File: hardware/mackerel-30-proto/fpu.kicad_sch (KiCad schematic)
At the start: 10 parts, among them U11 MC68882

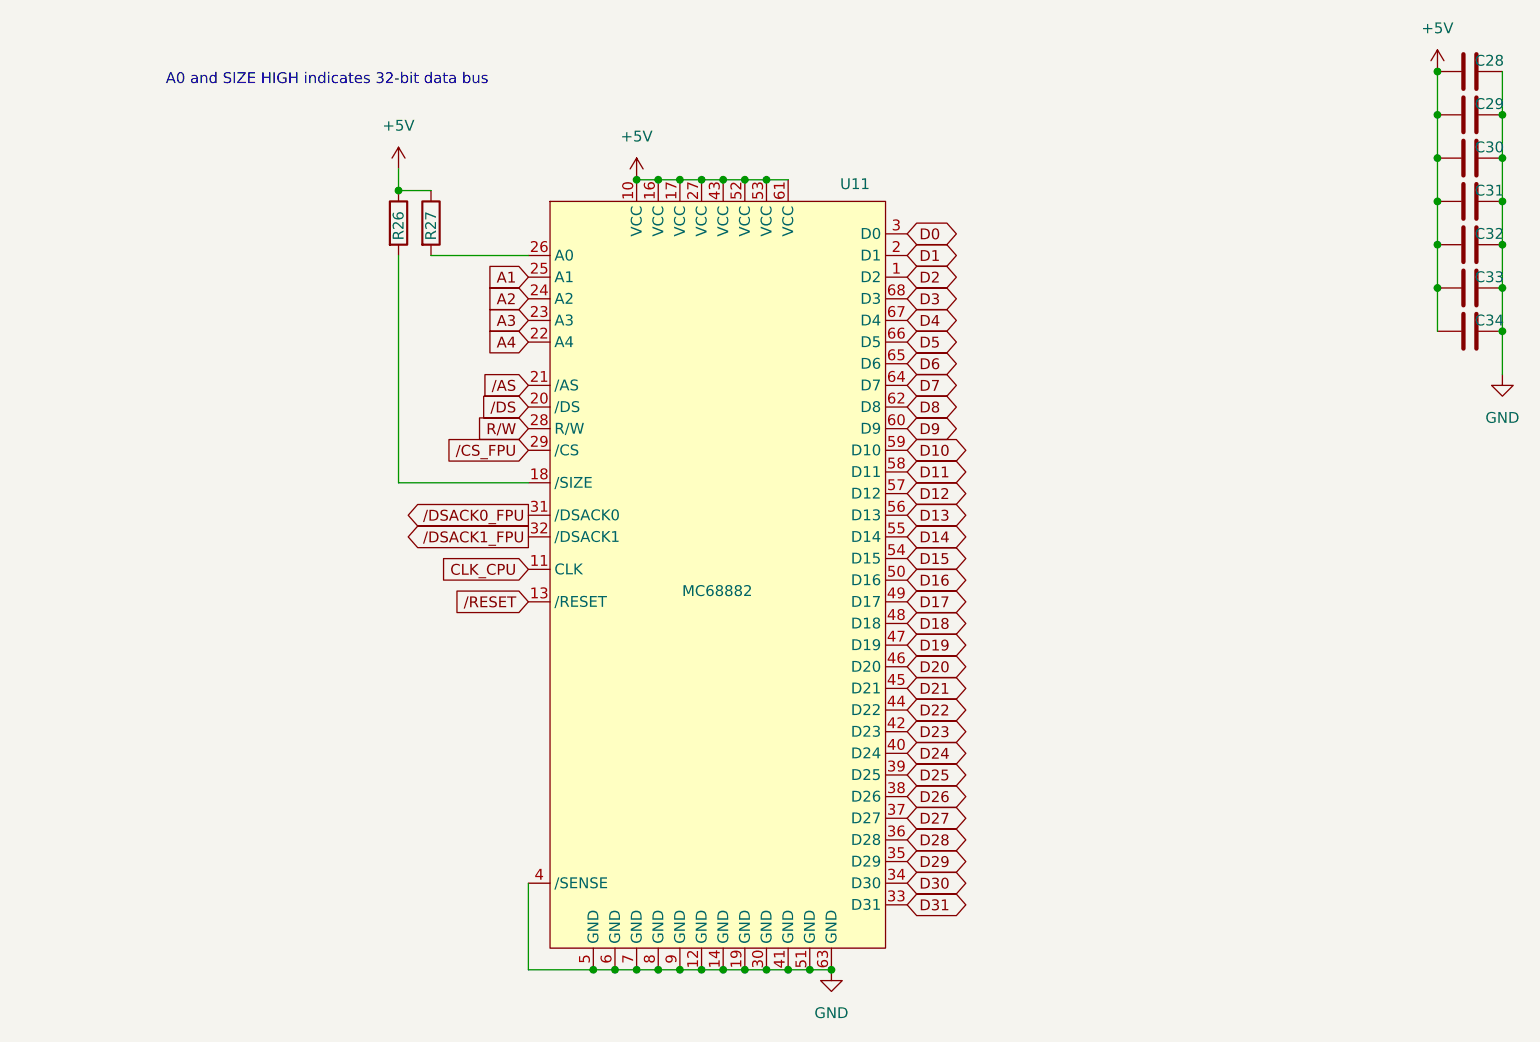
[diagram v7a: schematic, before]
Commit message: Rough routing of data bus to FPU and RAM
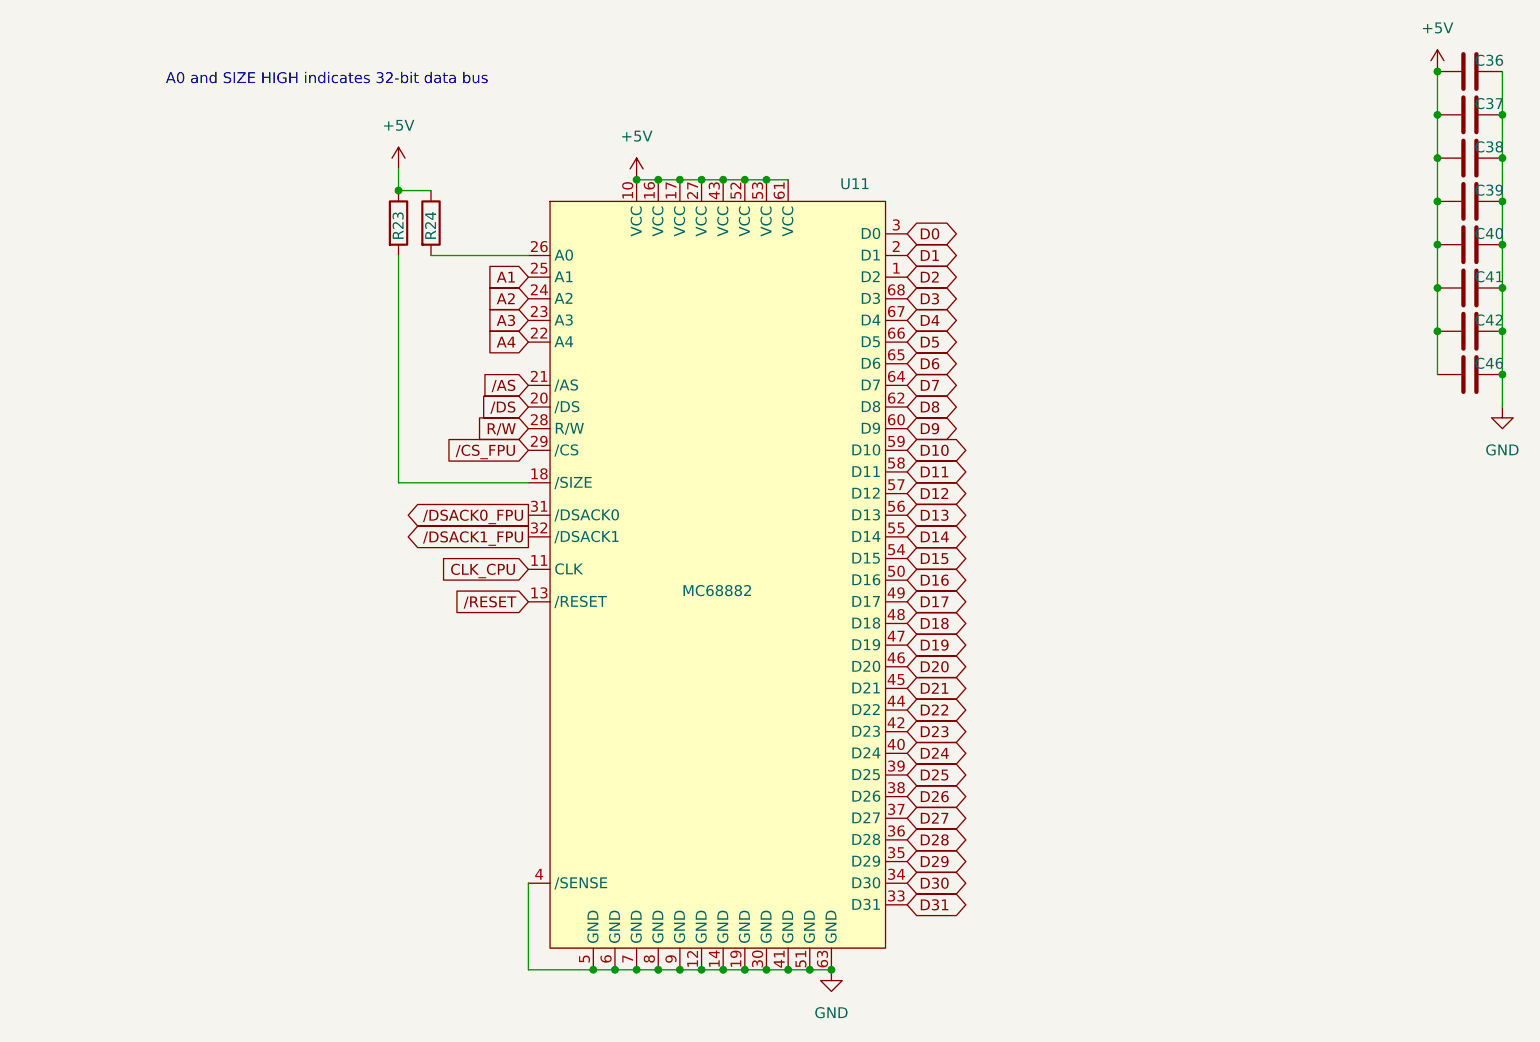
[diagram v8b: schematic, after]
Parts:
- added C46: 0.1uF, Capacitor_THT:C_Disc_D4.3mm_W1.9mm_P5.00mm, symbol Device:C
- renumbered C28 to C36, C29 to C37, C30 to C38, C31 to C39, C32 to C40, C33 to C41, C34 to C42, R26 to R23, R27 to R24
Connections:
- net +5V: now also C46.1
- net GND: now also C46.2
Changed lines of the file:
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@@
+	)
+	(junction
+		(at 186.69 71.12)
+		(diameter 0)
+		(color 0 0 0 0)
 	)
 	(junction
@@
 	)
 	(junction
+		(at 179.07 66.04)
+		(diameter 0)
+		(color 0 0 0 0)
+	)
+	(junction
 		(at 107.95 140.97)
 		(diameter 0)
@@
 	(wire
 		(pts
+			(xy 179.07 66.04) (xy 179.07 71.12)
+		)
+		(stroke
+			(width 0)
+			(type default)
+		)
+	)
+	(wire
+		(pts
 			(xy 186.69 35.56) (xy 186.69 40.64)
 		)
@@
 		(pts
 			(xy 92.71 48.26) (xy 95.25 48.26)
+		)
+		(stroke
+			(width 0)
+			(type default)
+		)
+	)
+	(wire
+		(pts
+			(xy 186.69 74.93) (xy 186.69 71.12)
 		)
 		(stroke
@@
 		(dnp no)
 		(fields_autoplaced yes)
-		(property "Reference" "#PWR068"
+		(property "Reference" "#PWR070"
 			(at 57.15 50.8 0)
 			(effects
@@
 			(project ""
 				(path "/9307474f-ec99-494d-b4c9-fbd0b10ce86a/a9f13681-faa6-4706-8ec9-421e908e3ee4"
-					(reference "#PWR068")
+					(reference "#PWR070")
 					(unit 1)
 				)
@@
 		(on_board yes)
 		(dnp no)
-		(property "Reference" "C29"
+		(property "Reference" "C37"
 			(at 185.166 39.37 90)
 			(effects
@@
 			(project "mackerel-30-proto"
 				(path "/9307474f-ec99-494d-b4c9-fbd0b10ce86a/a9f13681-faa6-4706-8ec9-421e908e3ee4"
-					(reference "C29")
+					(reference "C37")
 					(unit 1)
 				)
@@
 		(on_board yes)
 		(dnp no)
-		(property "Reference" "R27"
+		(property "Reference" "R24"
 			(at 60.96 55.372 90)
 			(effects
@@
 			(project "mackerel-30-proto"
 				(path "/9307474f-ec99-494d-b4c9-fbd0b10ce86a/a9f13681-faa6-4706-8ec9-421e908e3ee4"
-					(reference "R27")
+					(reference "R24")
 					(unit 1)
 				)
@@
 		(dnp no)
 		(fields_autoplaced yes)
-		(property "Reference" "#PWR071"
+		(property "Reference" "#PWR073"
 			(at 179.07 39.37 0)
 			(effects
@@
 			(project "mackerel-30-proto"
 				(path "/9307474f-ec99-494d-b4c9-fbd0b10ce86a/a9f13681-faa6-4706-8ec9-421e908e3ee4"
-					(reference "#PWR071")
+					(reference "#PWR073")
 					(unit 1)
 				)
@@
 		(dnp no)
 		(fields_autoplaced yes)
-		(property "Reference" "#PWR070"
+		(property "Reference" "#PWR072"
 			(at 107.95 147.32 0)
 			(effects
@@
 			(project ""
 				(path "/9307474f-ec99-494d-b4c9-fbd0b10ce86a/a9f13681-faa6-4706-8ec9-421e908e3ee4"
-					(reference "#PWR070")
+					(reference "#PWR072")
 					(unit 1)
 				)
@@
 		(dnp no)
 		(fields_autoplaced yes)
-		(property "Reference" "#PWR069"
+		(property "Reference" "#PWR071"
 			(at 85.09 52.07 0)
 			(effects
@@
 			(project ""
 				(path "/9307474f-ec99-494d-b4c9-fbd0b10ce86a/a9f13681-faa6-4706-8ec9-421e908e3ee4"
-					(reference "#PWR069")
+					(reference "#PWR071")
 					(unit 1)
 				)
@@
 		(on_board yes)
 		(dnp no)
-		(property "Reference" "C32"
+		(property "Reference" "C40"
 			(at 185.166 54.61 90)
 			(effects
@@
 			(project "mackerel-30-proto"
 				(path "/9307474f-ec99-494d-b4c9-fbd0b10ce86a/a9f13681-faa6-4706-8ec9-421e908e3ee4"
-					(reference "C32")
+					(reference "C40")
 					(unit 1)
 				)
@@
 		(on_board yes)
 		(dnp no)
-		(property "Reference" "R26"
+		(property "Reference" "R23"
 			(at 57.15 55.372 90)
 			(effects
@@
 			(project "mackerel-30-proto"
 				(path "/9307474f-ec99-494d-b4c9-fbd0b10ce86a/a9f13681-faa6-4706-8ec9-421e908e3ee4"
-					(reference "R26")
+					(reference "R23")
 					(unit 1)
 				)
@@
 	(symbol
 		(lib_id "power:GND")
-		(at 186.69 71.12 0)
+		(at 186.69 74.93 0)
 		(unit 1)
 		(exclude_from_sim no)
@@
 		(dnp no)
 		(fields_autoplaced yes)
-		(property "Reference" "#PWR072"
-			(at 186.69 77.47 0)
+		(property "Reference" "#PWR074"
+			(at 186.69 81.28 0)
 			(effects
 				(font
@@
 		)
 		(property "Value" "GND"
-			(at 186.69 76.2 0)
+			(at 186.69 80.01 0)
 			(effects
 				(font
@@
 		)
 		(property "Footprint" ""
-			(at 186.69 71.12 0)
+			(at 186.69 74.93 0)
 			(effects
 				(font
@@
 		)
 		(property "Datasheet" ""
-			(at 186.69 71.12 0)
+			(at 186.69 74.93 0)
 			(effects
 				(font
@@
 		)
 		(property "Description" "Power symbol creates a global label with name \"GND\" , ground"
-			(at 186.69 71.12 0)
+			(at 186.69 74.93 0)
 			(effects
 				(font
@@
 			(project ""
 				(path "/9307474f-ec99-494d-b4c9-fbd0b10ce86a/a9f13681-faa6-4706-8ec9-421e908e3ee4"
-					(reference "#PWR072")
+					(reference "#PWR074")
 					(unit 1)
 				)
@@
 		(on_board yes)
 		(dnp no)
-		(property "Reference" "C33"
+		(property "Reference" "C41"
 			(at 185.166 59.69 90)
 			(effects
@@
 			(project "mackerel-30-proto"
 				(path "/9307474f-ec99-494d-b4c9-fbd0b10ce86a/a9f13681-faa6-4706-8ec9-421e908e3ee4"
-					(reference "C33")
+					(reference "C41")
 					(unit 1)
 				)
@@
 		(on_board yes)
 		(dnp no)
-		(property "Reference" "C30"
+		(property "Reference" "C38"
 			(at 185.166 44.45 90)
 			(effects
@@
 			(project "mackerel-30-proto"
 				(path "/9307474f-ec99-494d-b4c9-fbd0b10ce86a/a9f13681-faa6-4706-8ec9-421e908e3ee4"
-					(reference "C30")
+					(reference "C38")
 					(unit 1)
 				)
@@
 		(on_board yes)
 		(dnp no)
-		(property "Reference" "C28"
+		(property "Reference" "C36"
 			(at 185.166 34.29 90)
 			(effects
@@
 			(project "mackerel-30-proto"
 				(path "/9307474f-ec99-494d-b4c9-fbd0b10ce86a/a9f13681-faa6-4706-8ec9-421e908e3ee4"
-					(reference "C28")
+					(reference "C36")
 					(unit 1)
 				)
@@
 		(on_board yes)
 		(dnp no)
-		(property "Reference" "C31"
+		(property "Reference" "C39"
 			(at 185.166 49.53 90)
 			(effects
@@
 			(project "mackerel-30-proto"
 				(path "/9307474f-ec99-494d-b4c9-fbd0b10ce86a/a9f13681-faa6-4706-8ec9-421e908e3ee4"
-					(reference "C31")
+					(reference "C39")
 					(unit 1)
 				)
@@
 		(on_board yes)
 		(dnp no)
-		(property "Reference" "C34"
+		(property "Reference" "C42"
 			(at 185.166 64.77 90)
 			(effects
@@
 			(project "mackerel-30-proto"
 				(path "/9307474f-ec99-494d-b4c9-fbd0b10ce86a/a9f13681-faa6-4706-8ec9-421e908e3ee4"
-					(reference "C34")
+					(reference "C42")
 					(unit 1)
 				)
+			)
+		)
+	)
+	(symbol
+		(lib_id "Device:C")
+		(at 182.88 71.12 90)
+		(unit 1)
+		(exclude_from_sim no)
+		(in_bom yes)
+		(on_board yes)
+		(dnp no)
+		(property "Reference" "C46"
+			(at 185.166 69.85 90)
+			(effects
+				(font
+					(size 1.27 1.27)
+				)
+			)
+		)
+		(property "Value" "0.1uF"
+			(at 182.88 66.04 90)
+			(effects
+				(font
+					(size 1.27 1.27)
+				)
+				(hide yes)
+			)
+		)
+		(property "Footprint" "Capacitor_THT:C_Disc_D4.3mm_W1.9mm_P5.00mm"
+			(at 186.69 70.1548 0)
+			(effects
+				(font
+					(size 1.27 1.27)
+				)
+				(hide yes)
+			)
+		)
+		(property "Datasheet" "~"
+			(at 182.88 71.12 0)
+			(effects
+				(font
+					(size 1.27 1.27)
+				)
+				(hide yes)
+			)
+		)
+		(property "Description" "Unpolarized capacitor"
+			(at 182.88 71.12 0)
+			(effects
+				(font
+					(size 1.27 1.27)
+				)
+				(hide yes)
+			)
+		)
+		(pin "2"
+		)
+		(pin "1"
+		)
+		(instances
+			(project "mackerel-30-proto"
+				(path "/9307474f-ec99-494d-b4c9-fbd0b10ce86a/a9f13681-faa6-4706-8ec9-421e908e3ee4"
+					(reference "C46")
+					(unit 1)
+				)
